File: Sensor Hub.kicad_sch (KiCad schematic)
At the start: 38 parts, among them J1 SWD, J2 SD_Card, SW1 SW_SPDT, SW2 SW_Push, U1 LM20BIM7, U2 STM32L100RBT6A_LQFP64, U3 LD_SSOP, U5 AM2320, U6 Type_C_USB4125, U7 APDS-9960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

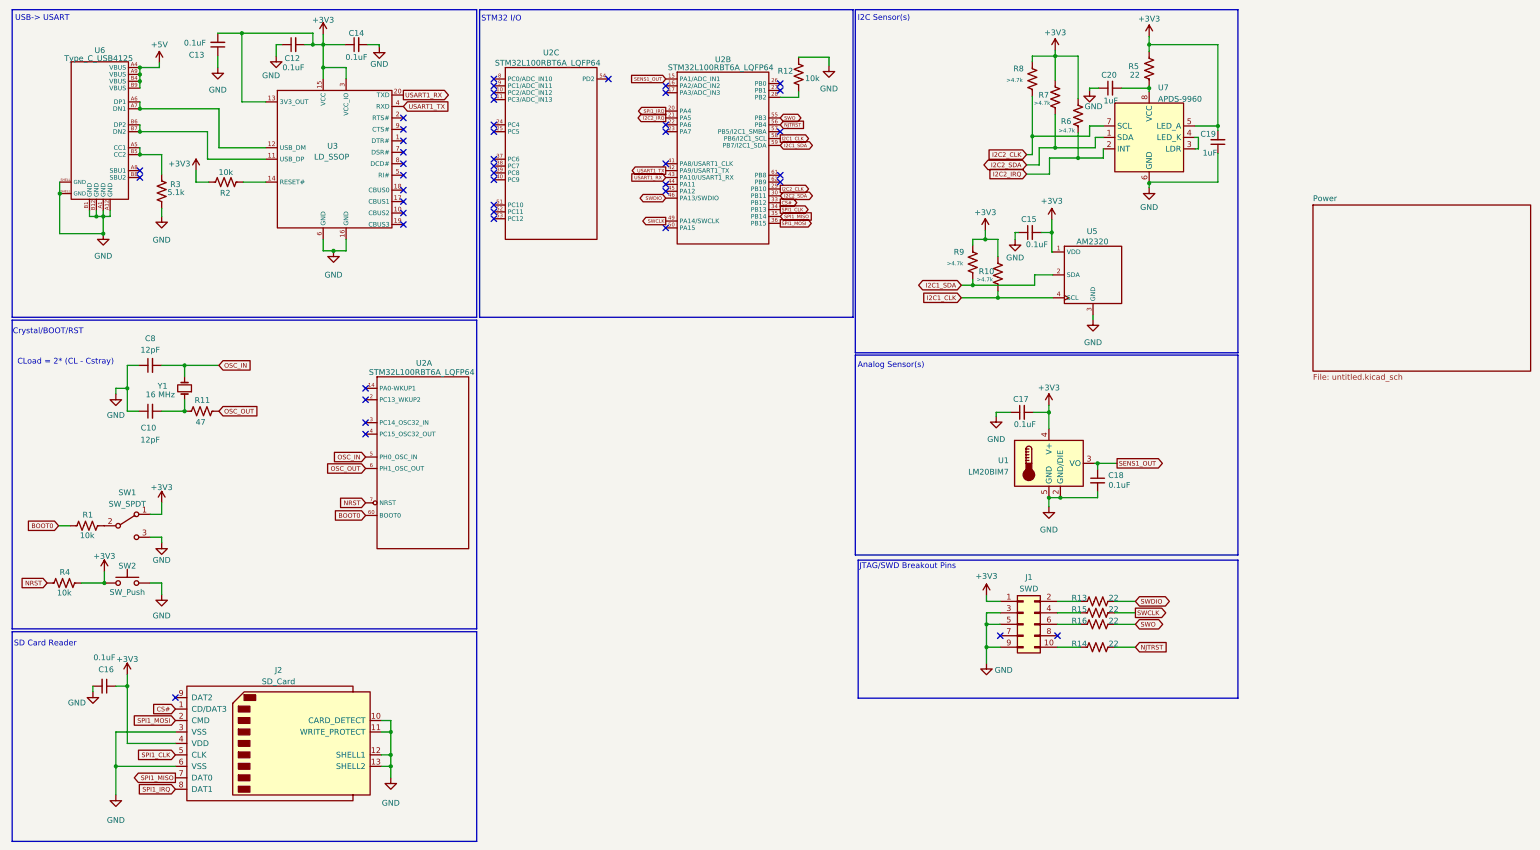
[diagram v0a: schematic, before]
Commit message: Update to schem
- Updated per Adi's feedback
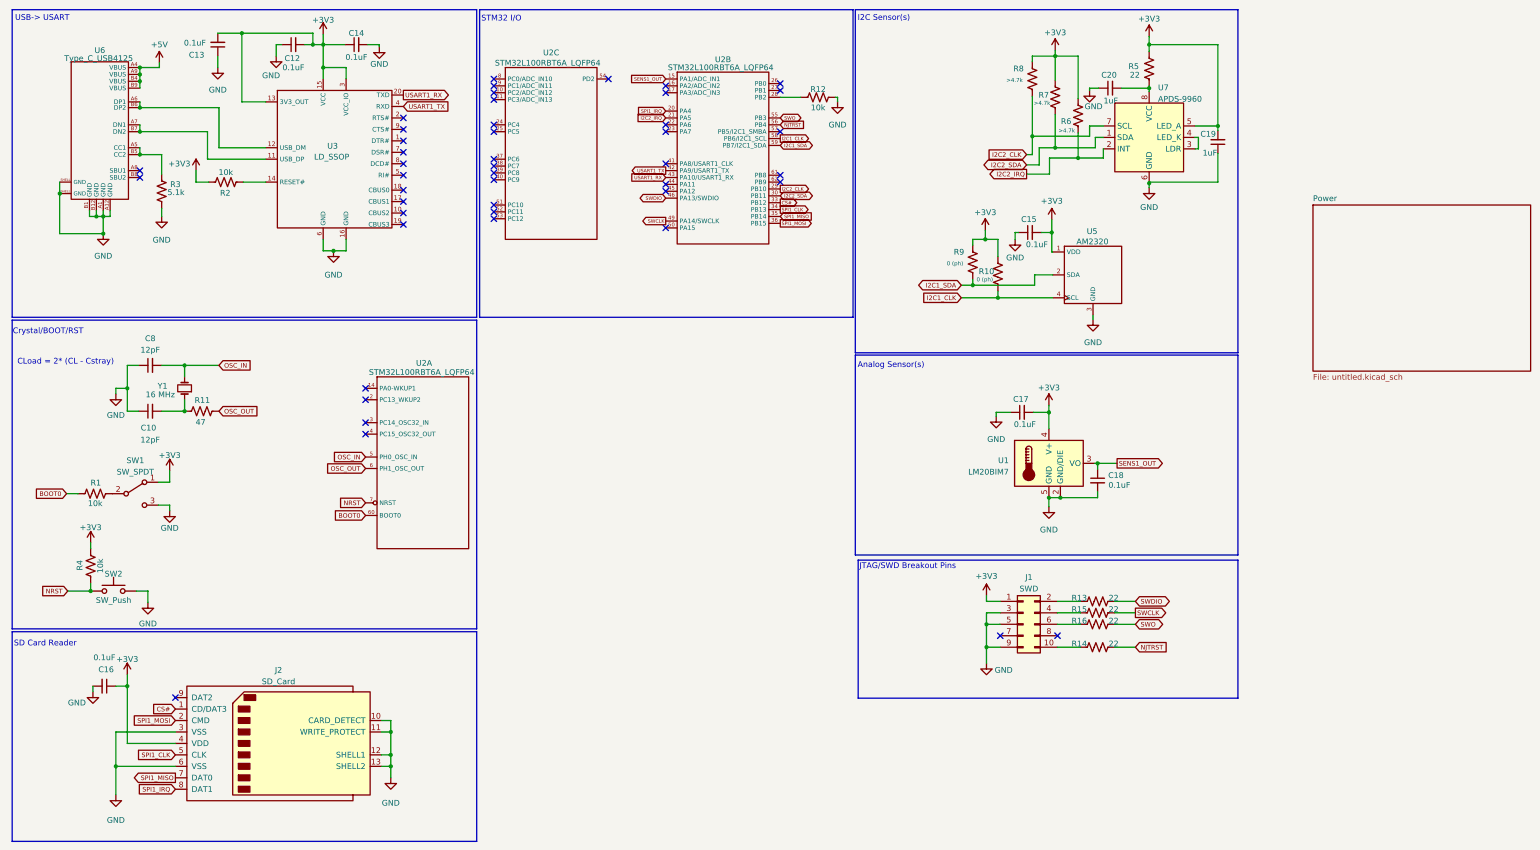
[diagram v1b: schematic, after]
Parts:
- R10, R9: value >4.7k -> 0 (ph)
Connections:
- net +3V3: no longer SW2.1
- net GND: now also R12.2; no longer R12.1
- net NRST: now also SW2.1
- net at U2.28 (PB2): now also R12.1; no longer R12.2
- net at U3.12 (USB_DM), U6.A6 (DP1): now also U6.B6 (DP2); no longer U6.A7 (DN1)
- net at U3.11 (USB_DP), U6.B7 (DN2): now also U6.A7 (DN1); no longer U6.B6 (DP2)
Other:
- moved on the sheet: R1, SW1, SW2

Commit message: Updated Schematic
- Added LTC4002 battery management IC
- Updated previous ICs to reflect given feedback
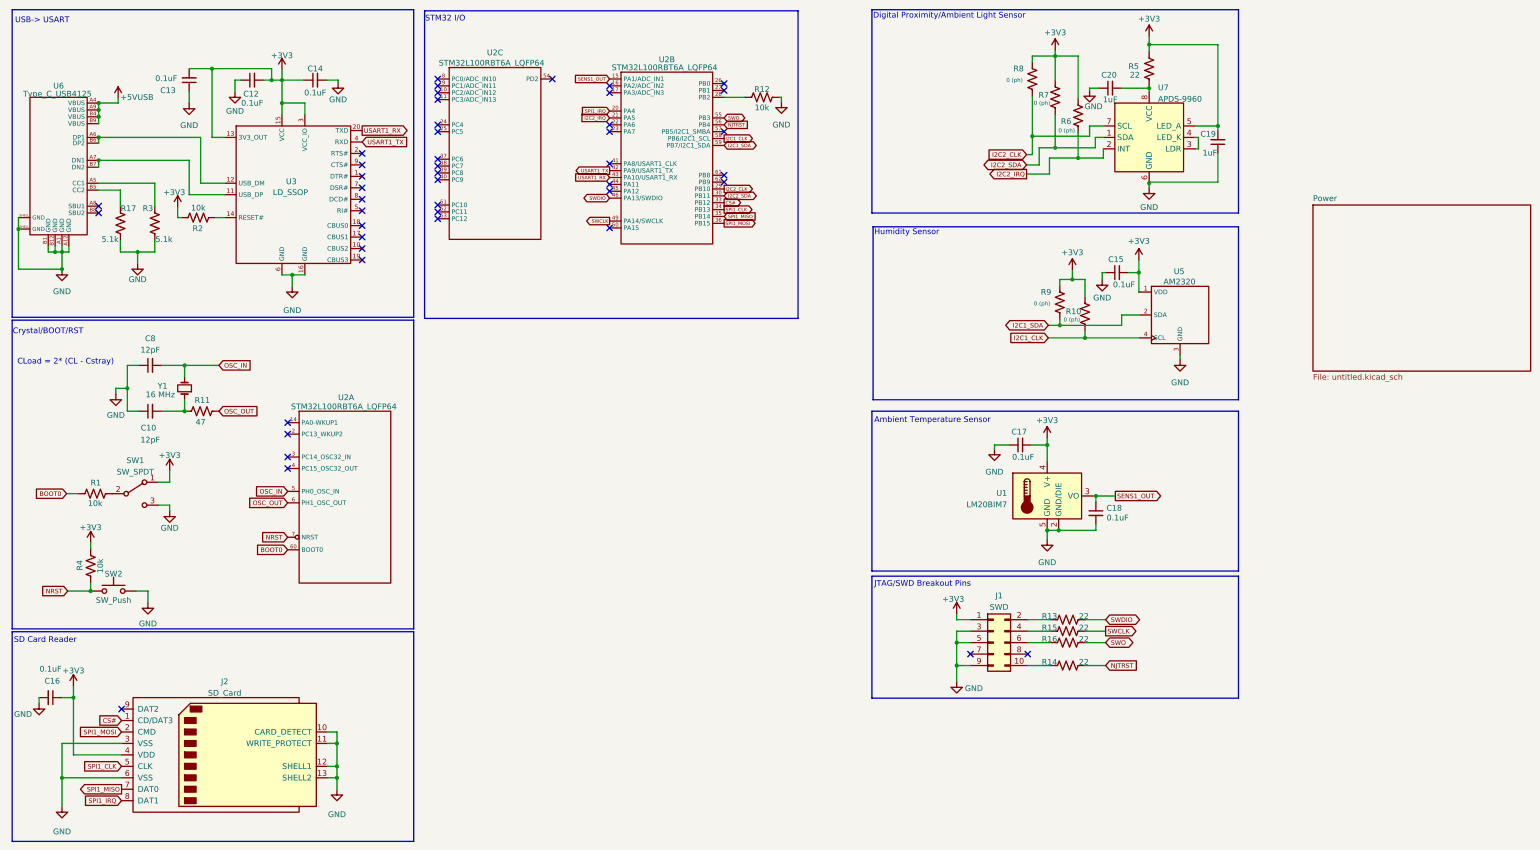
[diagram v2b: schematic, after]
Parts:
- added R17: 5.1k, Resistor_SMD:R_0805_2012Metric, symbol Device:R_US
- R6, R7, R8: value >4.7k -> 0 (ph)
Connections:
- net GND: now also R17.1
- net at R3.2, U6.A5 (CC1): no longer U6.B5 (CC2)
- new net: R17.2, U6.B5 (CC2)
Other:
- note added: "Ambient Temperature Sensor"
- note added: "Digital Proximity/Ambient Light Sensor"
- note added: "Humidity Sensor"
- note removed: "Analog Sensor(s)"
- note removed: "I2C Sensor(s)"
- moved on the sheet: C12, C13, C14, C15, C16, C17, C18, J1, J2, R10, R12, R13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

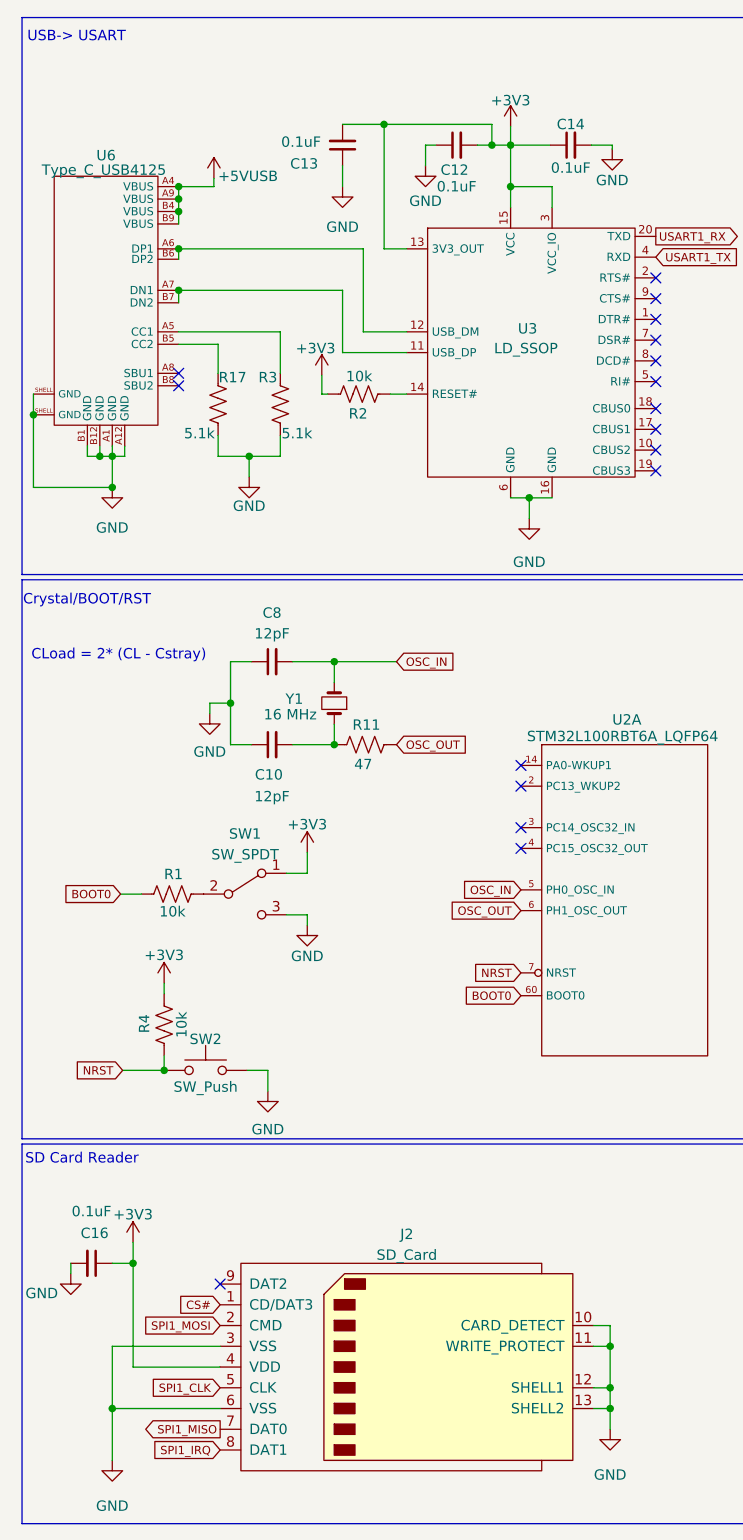
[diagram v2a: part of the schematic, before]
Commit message: Rev 0.3
+ Updated schematic to reflect utilization of USB-B micro instead of USB-C
+ Began initial layout of PCB

- Need to look into eFuse layout, as specified layout recommendation utilizes ground pours
- Need to update SD Card footprint as pads are not linked
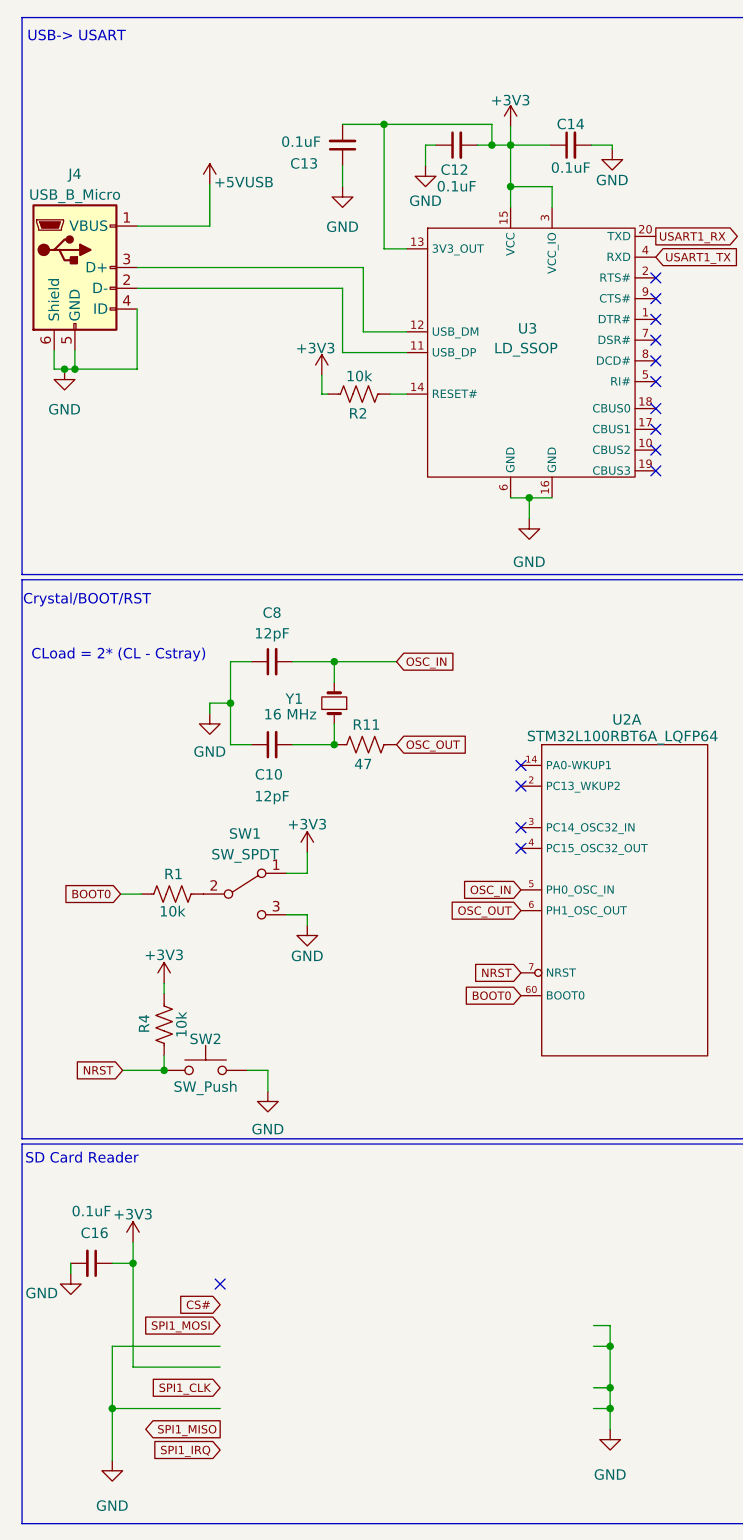
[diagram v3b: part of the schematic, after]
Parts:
- removed J2: SD_Card, Connector_Card:SD_Hirose_DM1AA_SF_PEJ82, symbol Connector:SD_Card
- removed R17, R3: 5.1k, Resistor_SMD:R_0805_2012Metric, symbol Device:R_US
- removed U6: Type_C_USB4125, Connector_USB:USB_C_Receptacle_G-Switch_GT-USB-7010ASV, symbol USB Receptacle:Type_C_USB4125
- added J4: USB_B_Micro, Connector_USB:USB_Micro-B_Amphenol_10118194_Horizontal, symbol Connector:USB_B_Micro
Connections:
- net +5V: now also J4.1 (VBUS)
- net GND: now also J4.4 (ID), J4.5 (GND), J4.6 (Shield)
- net at U3.12 (USB_DM): now also J4.3 (D+)
- net at U3.11 (USB_DP): now also J4.2 (D-)
- no-connect marks 46 -> 44

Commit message: Rev 1.0
+ Initial PCB board completed
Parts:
- added J2: SD_Card, Connector_Card:SD_Hirose_DM1AA_SF_PEJ82, symbol Connector:SD_Card
- U5: footprint Connector_PinSocket_2.00mm:PinSocket_1x04_P2.00mm_Horizontal -> Connector_PinSocket_2.00mm:PinSocket_1x04_P2.00mm_Vertical
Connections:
- net +3V3: now also J2.4 (VDD)
- net CS#: now also J2.1 (CD/DAT3)
- net GND: now also J2.10 (CARD_DETECT), J2.11 (WRITE_PROTECT), J2.12 (SHELL1), J2.13 (SHELL2), J2.3 (VSS), J2.6 (VSS)
- net SPI1_CLK: now also J2.5 (CLK)
- net SPI1_IRQ: now also J2.8 (DAT1)
- net SPI1_MISO: now also J2.7 (DAT0)
- net SPI1_MOSI: now also J2.2 (CMD)
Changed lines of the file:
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@@
       (effects (font (size 1.27 1.27)))
     )
-    (property "Footprint" "Connector_PinSocket_2.00mm:PinSocket_1x04_P2.00mm_Horizontal" (at 271.526 80.264 0)
+    (property "Footprint" "Connector_PinSocket_2.00mm:PinSocket_1x04_P2.00mm_Vertical" (at 271.526 80.264 0)
       (effects (font (size 1.27 1.27)) hide)
     )
@@
         )
       )
+    )
+  )
+  (symbol (lib_id "Connector:SD_Card") (at 59.69 177.8 0) (unit 1)
+    (in_bom yes) (on_board yes) (dnp no) (fields_autoplaced)
+    (property "Reference" "J2" (at 59.69 161.29 0)
+      (effects (font (size 1.27 1.27)))
+    )
+    (property "Value" "SD_Card" (at 59.69 163.83 0)
+      (effects (font (size 1.27 1.27)))
+    )
+    (property "Footprint" "Connector_Card:SD_Hirose_DM1AA_SF_PEJ82" (at 59.69 177.8 0)
+      (effects (font (size 1.27 1.27)) hide)
+    )
+    (property "Datasheet" "http://portal.fciconnect.com/Comergent//fci/drawing/10067847.pdf" (at 59.69 177.8 0)
+      (effects (font (size 1.27 1.27)) hide)
+    )
+    (pin "1")
+    (pin "10")
+    (pin "11")
+    (pin "12")
+    (pin "13")
+    (pin "2")
+    (pin "3")
+    (pin "4")
+    (pin "5")
+    (pin "6")
+    (pin "7")
+    (pin "8")
+    (pin "9")
+    (instances
+      (project "Sensor Hub"
+        (path "/c4cdbb0f-2866-4a3f-8578-00adb185b068"
+          (reference "J2") (unit 1)
+        )
+      )

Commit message: Updated to Rev 1.1
+ Adjusted trace widths to appropriately fit IC pads while supporting wanted current and minimizing vdrop
+ Adjusted edge cuts of PCB to remove unnecessary areas
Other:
- title: (none) -> Sensor Hub
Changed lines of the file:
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@@
 (kicad_sch (version 20230121) (generator eeschema)
   (paper "A4")
+  (title_block
+    (title "Sensor Hub")
+    (date "2023-04-03")
+    (rev "1.1")
+  )
   (junction (at 244.856 82.55) (diameter 0) (color 0 0 0 0)
   )
